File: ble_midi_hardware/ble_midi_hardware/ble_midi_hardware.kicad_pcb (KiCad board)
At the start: 2 copper layers, 68.6 x 59.3 mm, 11 parts, among them J1 Conn_01x02_Socket, J2 ESP32_Left, J3 ESP32_Right, J4 Conn_To_Midi_Device, U1 74HC595, U2 74HC595, U3 LM1117MP-3.3, U4 LM1117MP-5.0

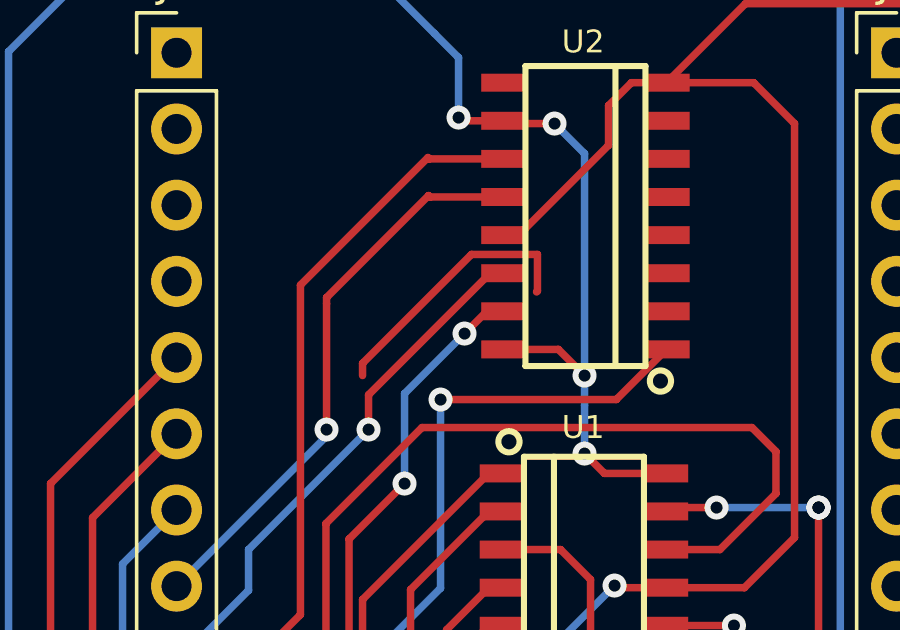
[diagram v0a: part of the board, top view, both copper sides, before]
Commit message: 移除孤立銅
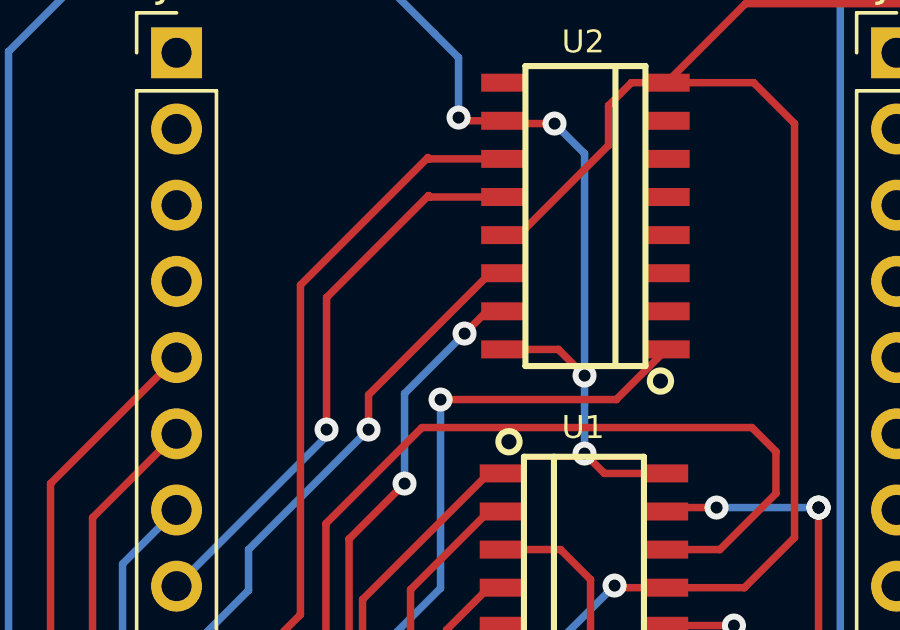
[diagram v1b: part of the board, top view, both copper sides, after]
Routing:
- net (no net): track 9.00 -> 0.00 mm
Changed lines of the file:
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@@
-	)
-	(segment
-		(start 113.4 72.593)
-		(end 117.0302 68.9628)
-		(width 0.25)
-		(layer "F.Cu")
-		(net 0)
-	)
-	(segment
-		(start 119.2302 68.9628)
-		(end 119.2302 70.1826)
-		(width 0.25)
-		(layer "F.Cu")
-		(net 0)
-	)
-	(segment
-		(start 119.2302 70.1826)
-		(end 119.2 70.2128)
-		(width 0.25)
-		(layer "F.Cu")
-		(net 0)
-	)
-	(segment
-		(start 117.0302 68.9628)
-		(end 119.2302 68.9628)
-		(width 0.25)
-		(layer "F.Cu")
-		(net 0)
-	)
-	(segment
-		(start 113.4 73)
-		(end 113.4 72.593)
-		(width 0.25)
-		(layer "F.Cu")
-		(net 0)
 	)
 	(segment

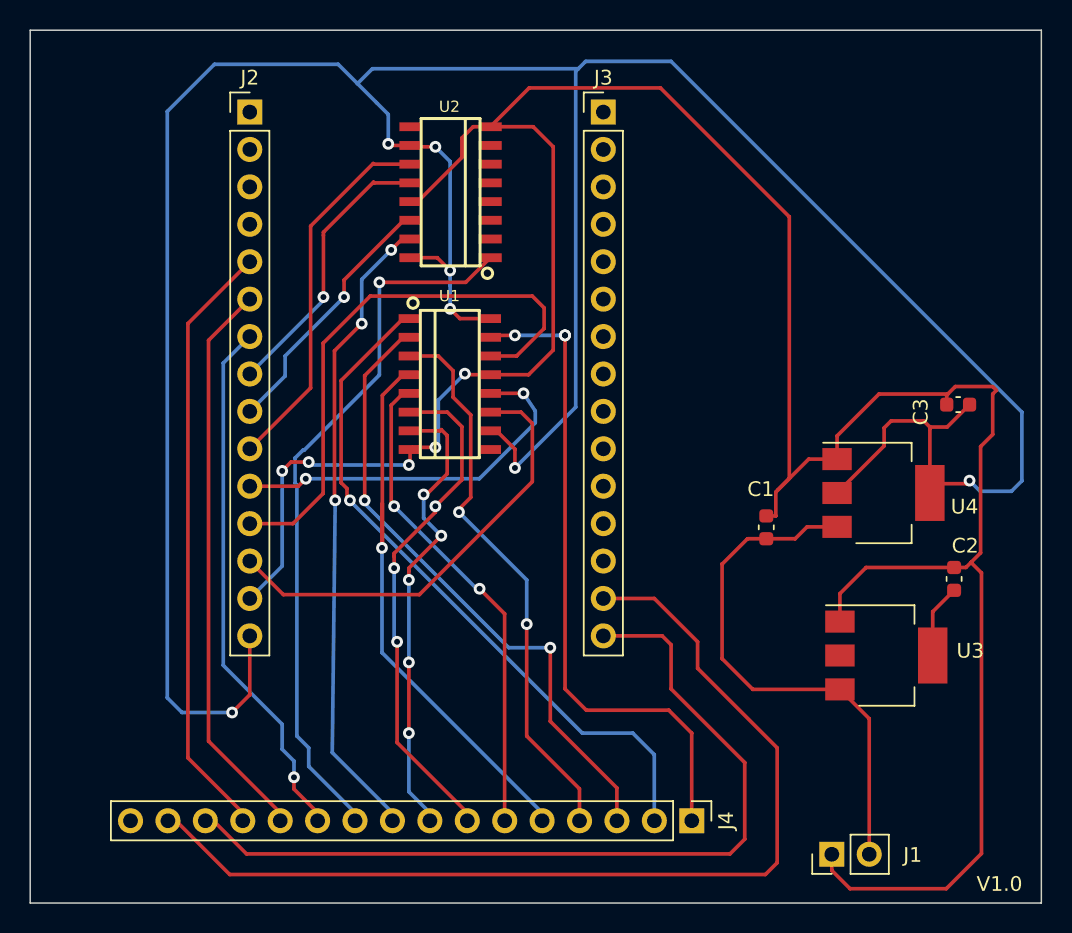
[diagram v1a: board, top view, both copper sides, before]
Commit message: 調整HC595供電5V為3.3V以及調整MCU INPUT GPIO pin腳位和部份走線
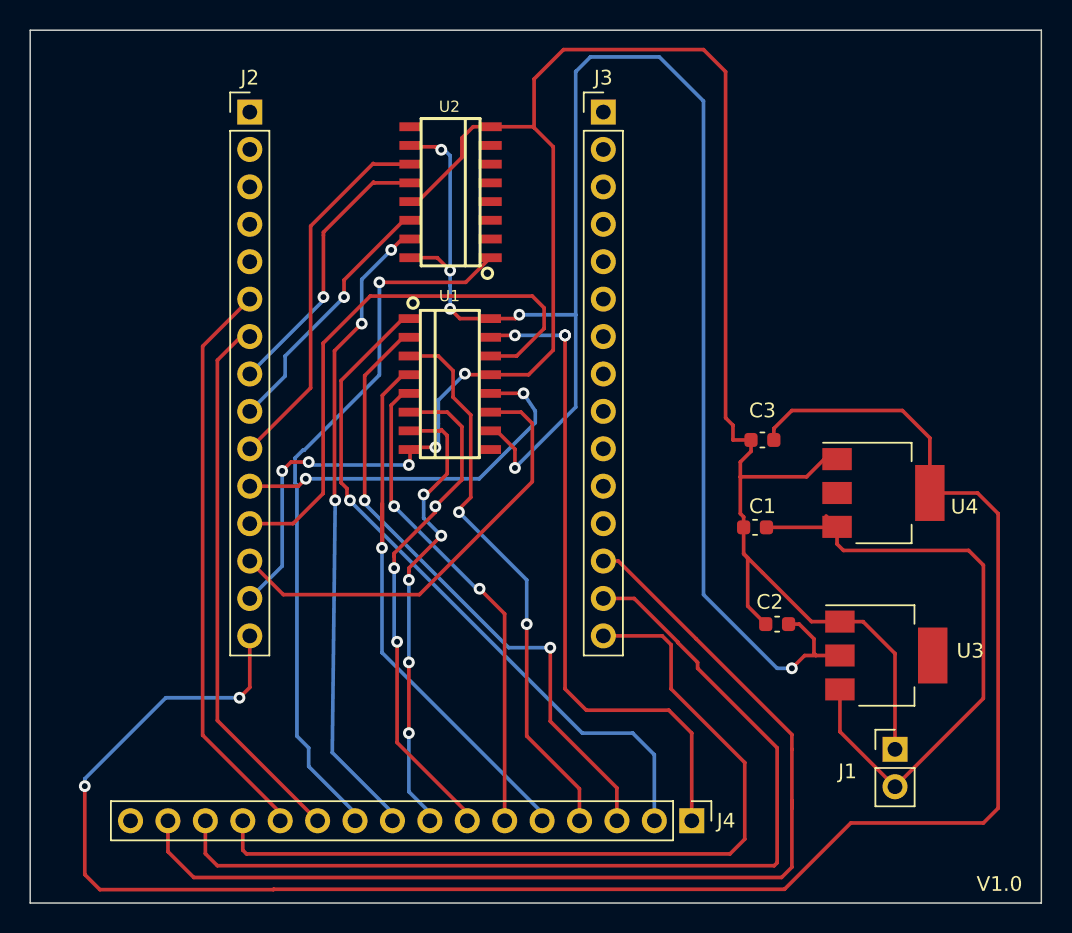
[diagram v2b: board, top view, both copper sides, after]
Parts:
- moved C3 13.5 mm to (142.0, 84.5)
- moved C2 12.4 mm to (143.0, 97.0), turned to 180 degrees
- moved J1 8.32 mm to (151.0, 105.5), turned to 0 degrees
- moved C1 0.76 mm to (141.5, 90.4), turned to 180 degrees
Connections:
- J2 pad 5: /IN3 -> unconnected-(J2-Pin_5-Pad5)
- J3 pad 13: unconnected-(J3-Pin_13-Pad13) -> /IN3
- J4 pad 13: /IN3 -> /IN4
- J4 pad 14: /IN4 -> /IN5
- J4 pad 15: /IN5 -> /IN3
- U1 pad 10: /5V -> /3.3V
- U1 pad 16: /5V -> /3.3V
- U2 pad 10: /5V -> /3.3V
- U2 pad 16: /5V -> /3.3V
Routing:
- net /3.3V: track 5.03 -> 116.5 mm, vias 0 -> 6
- net /5V: track 208.1 -> 131.0 mm, vias 7 -> 2
- net /GND: track 184.1 -> 145.7 mm
- net /IN3: track 40.7 -> 72.6 mm
- net /電源/VIN: track 36.2 -> 43.2 mm
- net /IN5: track 68.3 -> 65.5 mm
- net /IN4: track 58.3 -> 56.7 mm
- net /IN1: track 35.7 -> 36.9 mm, vias 1 -> 0

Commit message: 調整SCK2(GPIO25)、RCK2(GPIO26)和SDA2(GPIO27)的腳位位置和pcb走線
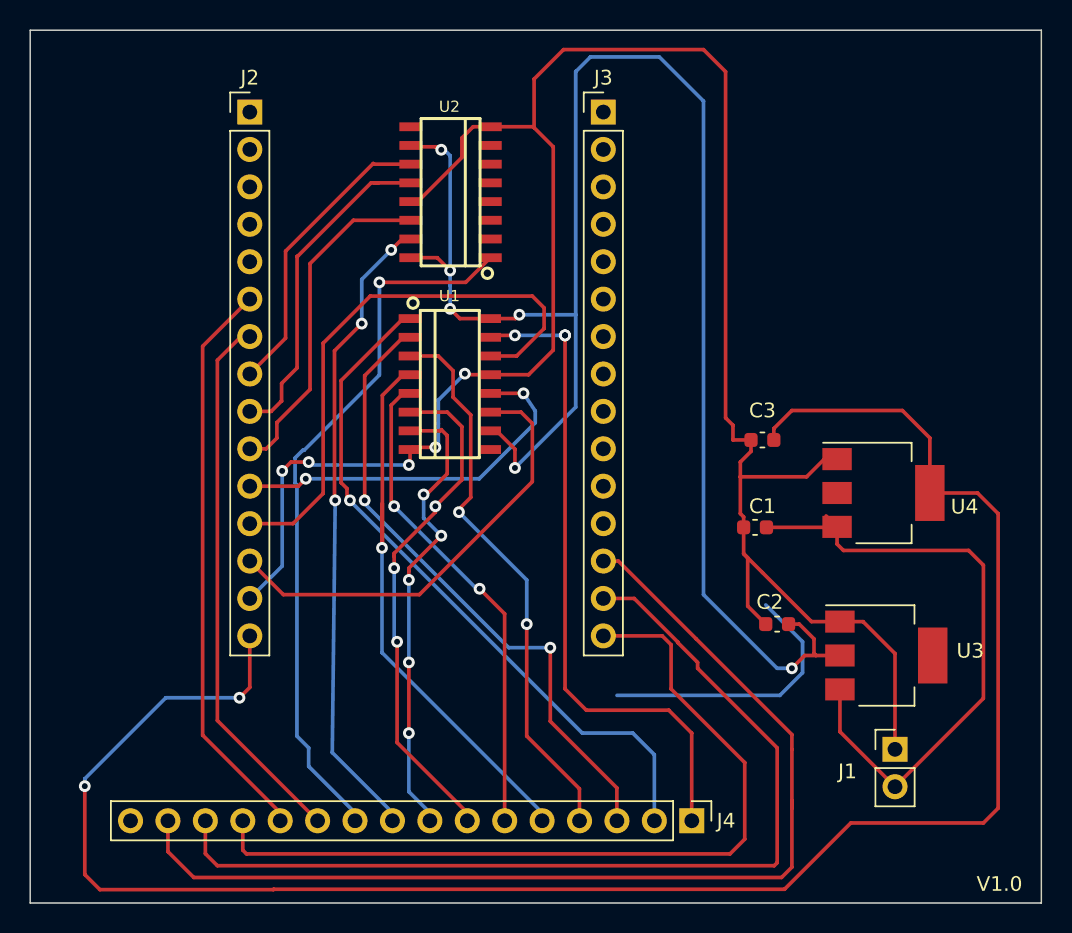
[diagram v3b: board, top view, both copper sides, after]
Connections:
- J2 pad 10: /SCK2 -> /SDA2
- J2 pad 8: /RCK2 -> /SCK2
- J2 pad 9: /SDA2 -> /RCK2
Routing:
- net (no net): track 0.00 -> 18.9 mm
- net /SDA2: track 17.8 -> 23.0 mm, vias 1 -> 0
- net /SCK2: track 25.4 -> 20.3 mm
- net /RCK2: track 19.2 -> 22.8 mm, vias 1 -> 0
